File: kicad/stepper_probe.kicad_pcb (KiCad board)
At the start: 2 copper layers, 33 x 42 mm, 55 parts, among them J1 Conn_01x04_Male, J2 Conn_01x04_Male, J3 BAT, J4 Serial Port, J5 SWD, J6 BAT, J7 Conn_01x01_Female, J8 Conn_01x01_Female, M1 Motor, SW1 SW_Push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

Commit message: Work in progress.
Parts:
- removed R1, R2, R3, R4: 10R, stepper_probe:R_0402_1005Metric_Pad0.72x0.64mm_HandSolder
- added F1: 500ma, stepper_probe:Fuse_0402, F.Cu at (141.3, 111.5)
- added F2: 500ma, stepper_probe:Fuse_0402, F.Cu at (143.7, 111.5)
- added F3: 500ma, stepper_probe:Fuse_0402, F.Cu at (146.5, 111.5)
- added F4: 500ma, stepper_probe:Fuse_0402, F.Cu at (149.0, 111.5)
- turned R13 to 180 degrees
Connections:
- D4 pad 1: Net-(C7-Pad1) -> Net-(D4-Pad1)
- D5 pad 1: Net-(C7-Pad1) -> Net-(D4-Pad1)
- R13 pad 1: Net-(R13-Pad1) -> Net-(C7-Pad1)
- R13 pad 2: Net-(C7-Pad1) -> Net-(D4-Pad1)
- U4 pad 1: Net-(R13-Pad1) -> Net-(C7-Pad1)
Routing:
- net Net-(D4-Pad1): track 0.00 -> 11.3 mm
- net Net-(C7-Pad1): track 29.5 -> 19.7 mm
- net Net-(R13-Pad1): track 2.95 -> 0.00 mm
- net Net-(J4-Pad2): track 18.2 -> 17.4 mm
- net Net-(C5-Pad1): track 5.72 -> 5.01 mm
- net GND: track 72.9 -> 72.3 mm

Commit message: Minor clean ups.
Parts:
- removed D4, D5: MB1S, stepper_probe:DIODE_BRIDGE
- removed D6: 1N5819WS, stepper_probe:D_SOD-323_HandSoldering
- removed F1, F2, F3, F4: 500ma, stepper_probe:Fuse_0402
- removed J7: Conn_01x01_Female, stepper_probe:BAT_PLUS_PAD
- removed J8: Conn_01x01_Female, stepper_probe:BAT_MINUS_PAD
- removed R13: 0R, stepper_probe:R_0402_1005Metric_Pad0.72x0.64mm_HandSolder
- added Q1: PJA3439, Package_TO_SOT_SMD:SOT-23, F.Cu at (148.6, 107.6)
- added R1: 300k, stepper_probe:R_0402_1005Metric_Pad0.72x0.64mm_HandSolder, F.Cu at (148.6, 104.7)
- J3: footprint stepper_probe:PinHeader_1x02_P2.54mm_Vertical -> stepper_probe:connector_2pins_horizontal
- moved J3 20.4 mm to (144.0, 102.0), turned to 180 degrees
- moved C9 3.25 mm to (143.2, 90.2)
- moved U5 1.54 mm to (145.2, 83.7)
- moved C10 1.53 mm to (143.1, 87.3)
- moved C11 1.49 mm to (143.1, 88.9)
- moved R14 0.66 mm to (145.8, 88.2)
- moved D3 0.50 mm to (147.9, 89.9)
- moved R5 0.50 mm to (147.9, 88.8)
- moved C12 0.23 mm to (147.9, 87.1)
- moved R10 0.22 mm to (145.4, 80.2)
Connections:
- J3 pad 2: /BAT+ -> Net-(J3-Pad2)
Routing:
- net /STEPPER3: track 28.2 -> 8.87 mm, vias 1 -> 0
- net /STEPPER1: track 32.5 -> 15.4 mm
- net GND: track 72.3 -> 89.1 mm, vias 21 -> 19
- net /STEPPER4: track 30.4 -> 14.2 mm, vias 1 -> 0
- net /STEPPER2: track 42.9 -> 29.1 mm
- net /BAT+: track 12.2 -> 0.00 mm
- net Net-(D4-Pad1): track 11.3 -> 0.00 mm
- net Net-(J3-Pad2): track 0.00 -> 8.05 mm
- net Net-(C7-Pad1): track 19.7 -> 14.9 mm
- net +3V3: track 75.8 -> 79.2 mm
- net Net-(D4-Pad3): track 1.97 -> 0.00 mm
- net Net-(D5-Pad3): track 1.96 -> 0.00 mm
- net Net-(D4-Pad4): track 1.92 -> 0.00 mm
- net Net-(D5-Pad4): track 1.91 -> 0.00 mm
- net /SCL: track 26.9 -> 28.4 mm
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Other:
- board text removed: "9V BAT ZERO CALIB."

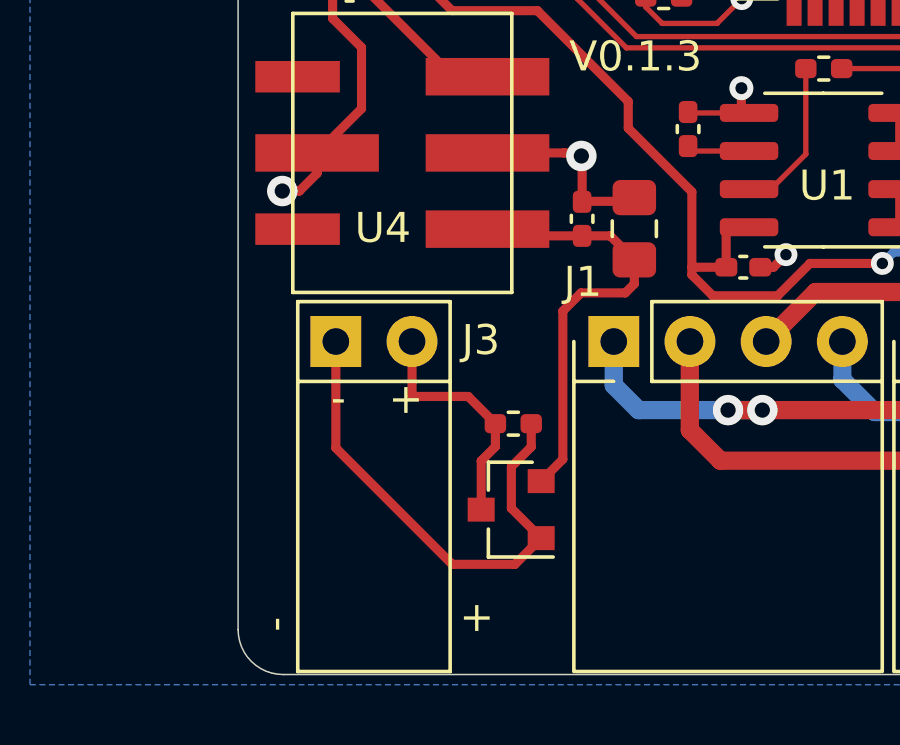
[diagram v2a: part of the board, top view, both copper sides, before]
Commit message: Cleaned up power in header.
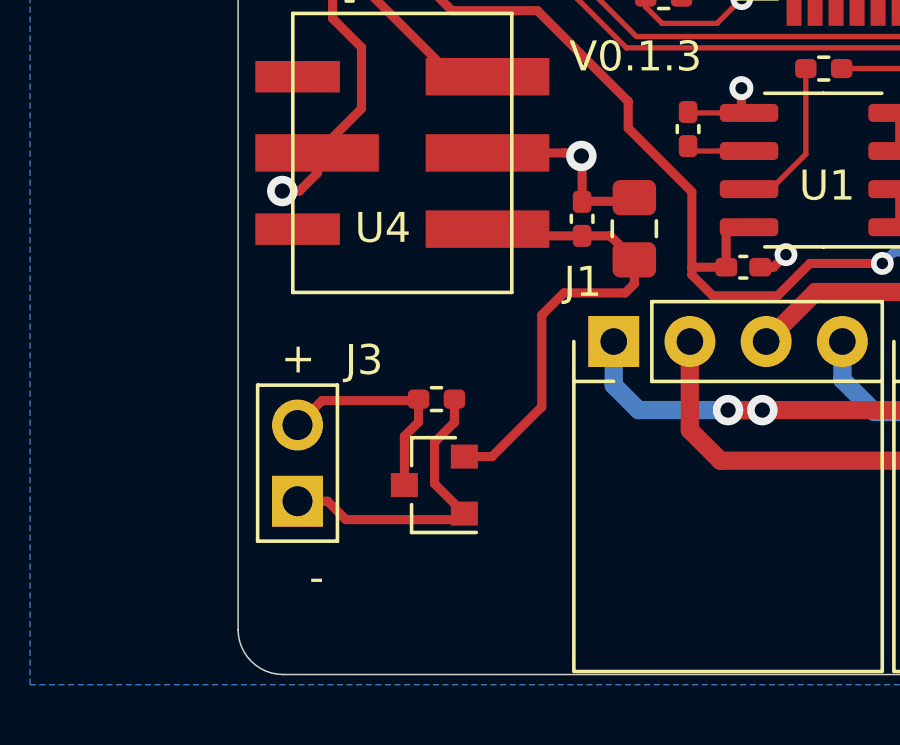
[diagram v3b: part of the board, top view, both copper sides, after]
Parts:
- J3: footprint stepper_probe:connector_2pins_horizontal -> stepper_probe:PinHeader_1x02_P2.54mm_Vertical_JLCPCB_SMD
- J6: value BAT -> Reset header
- Q1: footprint Package_TO_SOT_SMD:SOT-23 -> stepper_probe:SOT-23_JLCPCB
- moved J3 4.79 mm to (141.5, 106.0), turned to 90 degrees
- moved R1 2.69 mm to (146.1, 103.9)
- moved Q1 2.69 mm to (146.0, 106.7), turned to 0 degrees
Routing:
- net GND: track 89.1 -> 82.7 mm
- net Net-(C7-Pad1): track 14.9 -> 16.0 mm
- net Net-(J3-Pad2): track 8.05 -> 7.45 mm

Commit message: Minor change of 'DNI' to 'DNP' for consistency.
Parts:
- C13, C14: value DNI -> DNP

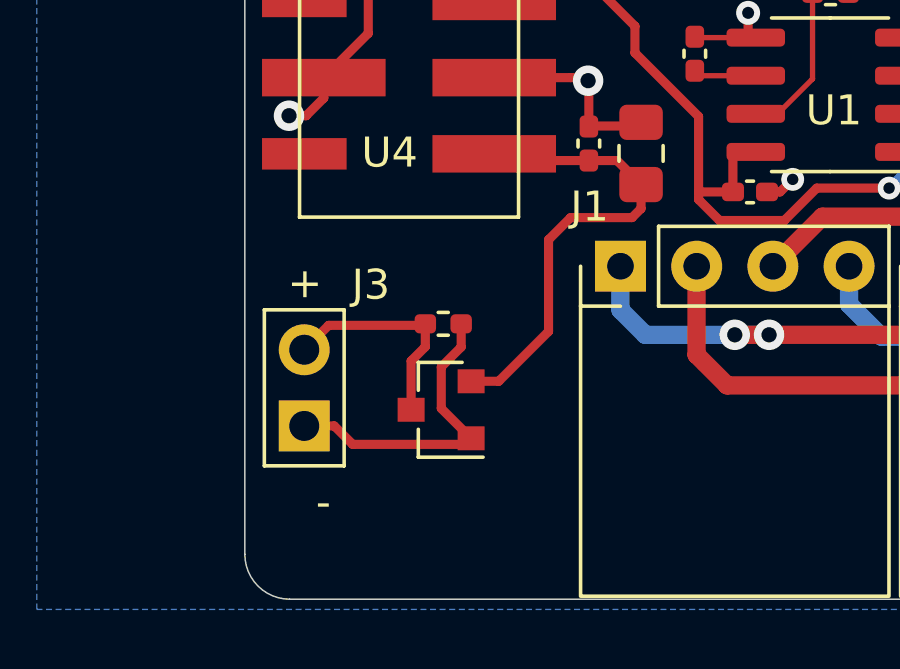
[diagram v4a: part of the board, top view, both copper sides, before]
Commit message: Added zener protection
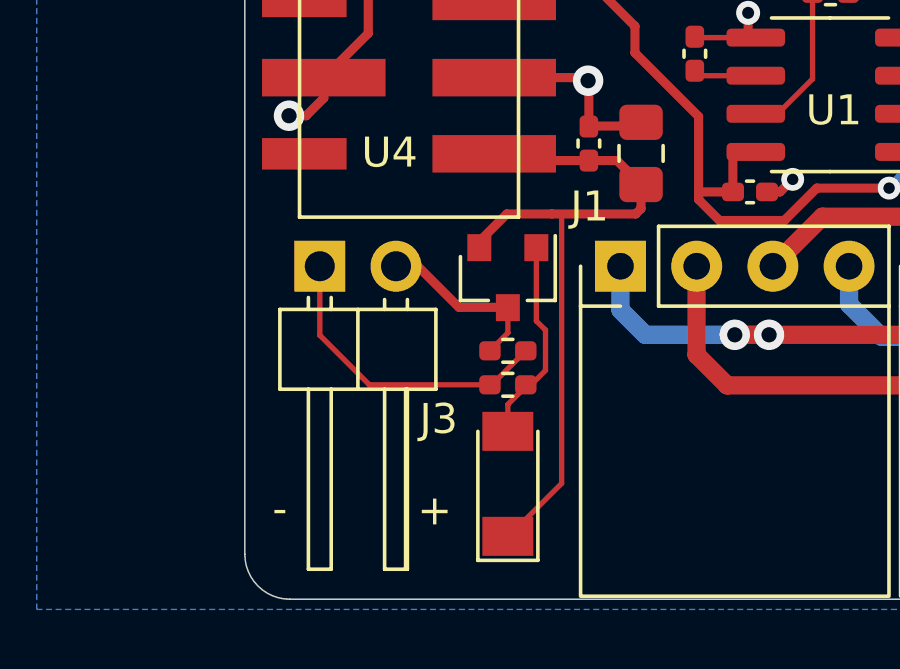
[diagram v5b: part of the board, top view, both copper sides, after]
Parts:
- added D4: 5V6, Diode_SMD:D_MiniMELF, F.Cu at (148.2, 109.2)
- added R2: 20k, stepper_probe:R_0402_1005Metric_Pad0.72x0.64mm_HandSolder, F.Cu at (148.2, 105.9)
- J3: footprint stepper_probe:PinHeader_1x02_P2.54mm_Vertical_JLCPCB_SMD -> stepper_probe:PinHeader_1x02_P2.54mm_Horizontal_JLCPCB
- moved Q1 4.93 mm to (148.2, 102.3), turned to 90 degrees
- moved J3 4.43 mm to (143.2, 102.0), turned to 180 degrees
- moved R1 2.33 mm to (148.2, 104.8)
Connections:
- Q1 pad 1: GND -> Net-(D4-Pad2)
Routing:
- net Net-(C7-Pad1): track 16.0 -> 23.7 mm
- net Net-(D4-Pad2): track 0.00 -> 7.15 mm
- net Net-(J3-Pad2): track 7.45 -> 5.81 mm
